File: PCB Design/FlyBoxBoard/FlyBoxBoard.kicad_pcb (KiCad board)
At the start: 2 copper layers, 40 parts, among them J1 5V in from buck converter, J10 R SCREW TERMINAL, J11 G SCREW TERMINAL, J12 W SCREW TERMINAL, J13 IR SCREW TERMINAL, J14 LCD Screen, J15 SD card reader, J16 Resistor, J17 Resistor, J18 ESP 32 Left Side extra pinouts, J19 ESP 32 Left Side extra pinouts, J2 12V in from buck converter, J20 Transistor, J21 Logic Level LV pinouts, J22 Potentiometer, J23 Logic Level Left Side LV, J24 ESP 32 Right Side extra pinou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, J25 ESP 32 Right Side extra pinou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, J26 BuckPuck IR, J27 Logic Level Right Side HV, J28 Logic Level HV pinouts, J29 Resistor, J3 ESP 32 Left Side, J30 Resistor, J31 Resistor, J32 Resistor, J33 Resistor, J34 Resistor, J35 Transistor, J36 Transistor, J37 Transistor, J38 BuckPuck White, J39 BuckPuck Green, J4 Real Time Controller, J40 BuckPuck Red, J5 ESP 32 Right Side, J6 Extra pinouts 5V, J7 Extra pinouts 12V, J8 Extra pinouts GND, J9 FAN SCREW TERMINAL

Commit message: PCB progress
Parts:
- J16, J17, J29, J30, J31, J32, J33, J34: footprint Connector_PinSocket_2.54mm:PinSocket_1x02_P2.54mm_Vertical -> Connector_PinSocket_2.54mm:PinSocket_1x05_P2.54mm_Vertical
- moved J10 322.2 mm to (67.3, 22.9)
- moved J11 322.2 mm to (61.0, 21.6)
- moved J12 322.2 mm to (74.9, 20.3)
- moved J13 236.1 mm to (168.9, -74.9)
- moved J9 141.0 mm to (24.1, 29.2), turned to 90 degrees
- moved J30 119.4 mm to (115.6, 37.4)
- moved J35 118.2 mm to (133.4, 39.9)
- moved J38 117.9 mm to (144.8, 36.1)
- moved J37 115.7 mm to (133.3, 83.1)
- moved J33 115.6 mm to (120.7, 80.5)
- moved J34 114.6 mm to (115.6, 80.5)
- moved J40 114.4 mm to (144.8, 79.5)
- moved J29 112.6 mm to (120.7, 37.4)
- moved J1 108.1 mm to (133.3, 17.8)
- moved J20 86.6 mm to (129.5, 105.9)
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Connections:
- J16 pad 2: Net-(J16-Pad2) -> unconnected-(J16-Pad2)
- J17 pad 2: /HV4 -> unconnected-(J17-Pad2)
- J20 pad 3: Net-(J16-Pad2) -> Net-(J20-Pad3)
- J22 pad 2: Net-(J16-Pad2) -> Net-(J20-Pad3)
- J22 pad 3: Net-(J16-Pad2) -> Net-(J20-Pad3)
- J26 pad 4: Net-(J16-Pad2) -> Net-(J20-Pad3)
- J27 pad 2: /LV1 -> /HV1
- J29 pad 2: Net-(J29-Pad2) -> unconnected-(J29-Pad2)
- J30 pad 2: /HV1 -> unconnected-(J30-Pad2)
- J31 pad 2: Net-(J31-Pad2) -> unconnected-(J31-Pad2)
- J32 pad 2: /HV2 -> unconnected-(J32-Pad2)
- J33 pad 2: Net-(J33-Pad2) -> unconnected-(J33-Pad2)
- J34 pad 2: /HV3 -> unconnected-(J34-Pad2)
- J35 pad 3: Net-(J29-Pad2) -> Net-(J35-Pad3)
- J36 pad 3: Net-(J31-Pad2) -> Net-(J36-Pad3)
- J37 pad 3: Net-(J33-Pad2) -> Net-(J37-Pad3)
- J38 pad 4: Net-(J29-Pad2) -> Net-(J35-Pad3)
- J39 pad 4: Net-(J31-Pad2) -> Net-(J36-Pad3)
- J40 pad 4: Net-(J33-Pad2) -> Net-(J37-Pad3)
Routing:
- net /GND: track 0.00 -> 48.0 mm
- net Net-(J16-Pad2): track 44.3 -> 0.00 mm
- net Net-(J20-Pad3): track 0.00 -> 28.7 mm
- net Net-(J37-Pad3): track 0.00 -> 26.1 mm
- net Net-(J36-Pad3): track 0.00 -> 25.7 mm
- net Net-(J35-Pad3): track 0.00 -> 25.7 mm
- net Net-(J20-Pad2): track 0.00 -> 19.9 mm
- net Net-(J36-Pad2): track 0.00 -> 19.9 mm
- net Net-(J35-Pad2): track 0.00 -> 19.9 mm
- net Net-(J34-Pad1): track 0.00 -> 19.9 mm
- net Net-(J37-Pad1): track 0.00 -> 13.1 mm
- net Net-(J35-Pad1): track 0.00 -> 12.0 mm
- net Net-(J36-Pad1): track 0.00 -> 12.0 mm
- net Net-(J20-Pad1): track 25.9 -> 15.8 mm
- net Net-(J24-Pad3): track 6.59 -> 10.4 mm
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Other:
- board outline added: 149.9 x 120.6 mm

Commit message: Main PCB complete
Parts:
- moved J13 157.3 mm to (45.7, 22.9), turned to -90 degrees
- moved J8 12.7 mm to (91.5, 44.5)
- moved J15 11.7 mm to (57.1, 129.5), turned to -90 degrees
- moved J7 11.4 mm to (63.5, 44.5)
- moved J6 11.4 mm to (78.8, 44.5)
- moved J10 10.2 mm to (57.1, 22.9), turned to -90 degrees
- moved J11 7.73 mm to (68.6, 22.9), turned to -90 degrees
- moved J4 7.41 mm to (31.8, 54.6)
- moved J9 6.48 mm to (22.9, 22.8)
- moved J12 5.68 mm to (80.0, 22.9), turned to -90 degrees
- moved J14 2.62 mm to (77.5, 129.5)
- moved J1 2.54 mm to (133.3, 20.3)
- moved J2 2.54 mm to (111.8, 20.3)
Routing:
- net /5V: track 0.00 -> 358.7 mm, vias 0 -> 2
- net /12V: track 0.00 -> 297.1 mm
- net /3V3: track 0.00 -> 175.1 mm
- net /IR LED-: track 0.00 -> 157.1 mm, vias 0 -> 2
- net /IR LED+: track 0.00 -> 153.5 mm, vias 0 -> 2
- net /HV5: track 0.00 -> 132.2 mm
- net /R LED-: track 0.00 -> 128.2 mm, vias 0 -> 2
- net /R LED+: track 0.00 -> 124.9 mm, vias 0 -> 2
- net /D22: track 0.00 -> 119.9 mm, vias 0 -> 4
- net /D21: track 0.00 -> 115.3 mm, vias 0 -> 4
- net /G LED-: track 0.00 -> 96.4 mm, vias 0 -> 2
- net /G LED+: track 0.00 -> 93.4 mm, vias 0 -> 2
- net /W LED-: track 0.00 -> 74.6 mm, vias 0 -> 2
- net /W LED+: track 0.00 -> 71.8 mm, vias 0 -> 2
- net /HV1: track 0.00 -> 57.1 mm, vias 0 -> 2
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- added copper zone on B.Cu, net /GND
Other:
- board size 149.9 x 120.6 mm -> 148.6 x 119.4 mm
- board text added: "ESP 32"

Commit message: Finished IR and RGW board
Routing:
- net /3V3: track 175.1 -> 173.0 mm
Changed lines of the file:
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@@
     (pts (xy 31.5268 81.5882) (xy 56.9268 81.5882))
     (height -5.08)
-    (gr_text "25.4000 mm" (at 44.2268 74.7082) (layer "F.Fab")
+    (gr_text "1000.0000 mils" (at 44.2268 74.7082) (layer "F.Fab")
       (effects (font (size 1.5 1.5) (thickness 0.3)))
     )
@@
     (pts (xy 86.36 91.44) (xy 99.06 91.44))
     (height -6.35)
-    (gr_text "12.7000 mm" (at 92.71 83.94) (layer "F.Fab")
+    (gr_text "500.0000 mils" (at 92.71 83.94) (layer "F.Fab")
       (effects (font (size 1 1) (thickness 0.15)))
     )
@@
   (segment (start 114.3 17.78) (end 147.32 17.78) (width 0.635) (layer "F.Cu") (net 3))
   (segment (start 109.22 17.78) (end 111.76 20.32) (width 0.635) (layer "F.Cu") (net 3))
-  (segment (start 91.44 91.44) (end 86.36 91.44) (width 0.635) (layer "F.Cu") (net 4))
   (segment (start 76.2 123.19) (end 85.09 123.19) (width 0.635) (layer "F.Cu") (net 4))
   (segment (start 86.36 118.11) (end 86.36 114.3) (width 0.635) (layer "F.Cu") (net 4))
   (segment (start 58.42 130.81) (end 58.42 132.08) (width 0.635) (layer "F.Cu") (net 4))
-  (segment (start 92.71 92.71) (end 91.44 91.44) (width 0.635) (layer "F.Cu") (net 4))
+  (segment (start 92.71 110.8964) (end 92.71 92.71) (width 0.635) (layer "F.Cu") (net 4))
   (segment (start 58.42 132.08) (end 71.12 132.08) (width 0.635) (layer "F.Cu") (net 4))
   (segment (start 71.12 132.08) (end 74.93 128.27) (width 0.635) (layer "F.Cu") (net 4))
+  (segment (start 91.44 91.44) (end 86.36 91.44) (width 0.635) (layer "F.Cu") (net 4))
   (segment (start 19.05 120.65) (end 19.05 83.82) (width 0.635) (layer "F.Cu") (net 4))
   (segment (start 85.09 123.19) (end 86.36 121.92) (width 0.635) (layer "F.Cu") (net 4))
-  (segment (start 92.71 111.76) (end 92.71 92.71) (width 0.635) (layer "F.Cu") (net 4))
   (segment (start 74.93 128.27) (end 74.93 124.46) (width 0.635) (layer "F.Cu") (net 4))
-  (segment (start 86.36 118.11) (end 92.71 111.76) (width 0.635) (layer "F.Cu") (net 4))
+  (segment (start 89.3064 114.3) (end 92.71 110.8964) (width 0.635) (layer "F.Cu") (net 4))
   (segment (start 19.05 83.82) (end 21.59 81.28) (width 0.635) (layer "F.Cu") (net 4))
   (segment (start 86.36 121.92) (end 86.36 118.11) (width 0.635) (layer "F.Cu") (net 4))
+  (segment (start 86.36 114.3) (end 89.3064 114.3) (width 0.635) (layer "F.Cu") (net 4))
   (segment (start 52.336961 132.7245) (end 31.1245 132.7245) (width 0.635) (layer "F.Cu") (net 4))
   (segment (start 31.2186 81.28) (end 31.5268 81.5882) (width 0.635) (layer "F.Cu") (net 4))
@@
   (segment (start 74.93 124.46) (end 76.2 123.19) (width 0.635) (layer "F.Cu") (net 4))
   (segment (start 52.981461 132.08) (end 52.336961 132.7245) (width 0.635) (layer "F.Cu") (net 4))
+  (segment (start 92.71 92.71) (end 91.44 91.44) (width 0.635) (layer "F.Cu") (net 4))
   (segment (start 58.42 132.08) (end 52.981461 132.08) (width 0.635) (layer "F.Cu") (net 4))
   (segment (start 57.15 129.54) (end 58.42 130.81) (width 0.635) (layer "F.Cu") (net 4))

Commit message: Ordering Fixes
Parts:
- moved J8 3.81 mm to (91.5, 48.3)
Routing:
- net /12V: track 297.1 -> 294.1 mm
- net /5V: track 358.7 -> 360.1 mm

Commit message: Update FlyBoxBoard.kicad_pcb
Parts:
- J1: value 5V in from buck converter -> 5V in
- J10: value R SCREW TERMINAL -> RED
- J11: value G SCREW TERMINAL -> GREEN
- J12: value W SCREW TERMINAL -> WHITE
- J13: value IR SCREW TERMINAL -> INFRARED
- J14: value LCD Screen -> LCD
- J18: value ESP 32 Left Side extra pinouts -> ESP 32 Left Side extra pins
- J2: value 12V in from buck converter -> 12V in
- J28: value Logic Level HV pinouts -> Logic Level HV pins
- J9: value FAN SCREW TERMINAL -> FAN
- moved GND 3.81 mm to (91.5, 44.5)
- renumbered J7 to 12V, J6 to 5V, J8 to GND
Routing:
- net /5V: track 360.1 -> 339.0 mm
- net /HV5: track 132.2 -> 127.1 mm
- net /HV4: track 29.0 -> 24.2 mm
- net Net-(J20-Pad2): track 19.9 -> 16.6 mm
- net /IR LED-: track 157.1 -> 158.9 mm
- net /IR LED+: track 153.5 -> 154.8 mm
- net /12V: track 294.1 -> 293.2 mm
- net /D23: track 31.2 -> 30.4 mm
- net /D22: track 119.9 -> 120.7 mm
- net /W LED+: track 71.8 -> 71.0 mm

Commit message: Gerber Files
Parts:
- J16, J17, J29, J30, J31, J32, J33, J34: value Resistor -> 5K Ohms
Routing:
- net (no net): track 0.00 -> 12.7 mm
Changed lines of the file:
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@@
       (disableapertmacros false)
       (usegerberextensions false)
-      (usegerberattributes true)
+      (usegerberattributes false)
       (usegerberadvancedattributes true)
       (creategerberjobfile true)
@@
       (outputformat 1)
       (mirror false)
-      (drillshape 1)
+      (drillshape 0)
       (scaleselection 1)
-      (outputdirectory "")
+      (outputdirectory "../FlyBoxBoardGerber/")
     )
   )
@@
       (effects (font (size 1 1) (thickness 0.15)))
     )
-    (fp_text value "Resistor" (at 0 12.93) (layer "F.SilkS")
+    (fp_text value "5K Ohms" (at 0 12.93) (layer "F.SilkS")
       (effects (font (size 1 1) (thickness 0.15)))
     )
@@
       (effects (font (size 1 1) (thickness 0.15)))
     )
-    (fp_text value "Resistor" (at 0 12.93) (layer "F.SilkS")
+    (fp_text value "5K Ohms" (at 0 12.93) (layer "F.SilkS")
       (effects (font (size 1 1) (thickness 0.15)))
     )
@@
       (effects (font (size 1 1) (thickness 0.15)))
     )
-    (fp_text value "Resistor" (at -3.835 4.5362 90) (layer "F.SilkS")
+    (fp_text value "5K Ohms" (at -3.835 4.5362 90) (layer "F.SilkS")
       (effects (font (size 1 1) (thickness 0.15)))
     )
@@
       (effects (font (size 1 1) (thickness 0.15)))
     )
-    (fp_text value "Resistor" (at 0 12.7) (layer "F.SilkS")
+    (fp_text value "5K Ohms" (at 0 12.7) (layer "F.SilkS")
       (effects (font (size 1 1) (thickness 0.15)))
     )
@@
       (effects (font (size 1 1) (thickness 0.15)))
     )
-    (fp_text value "ESP 32 Right Side extra pinouts" (at 3.785 7.3118 -90) (layer "F.SilkS")
+    (fp_text value "ESP 32 Right Side extra pinouts" (at 3.15 -7.2932 -90) (layer "F.SilkS")
       (effects (font (size 1 1) (thickness 0.15)))
     )
@@
     (property "Sheetname" "")
     (attr through_hole)
-    (fp_text reference "J4" (at 0 -2.77) (layer "F.SilkS")
-      (effects (font (size 1 1) (thickness 0.15)))
-    )
-    (fp_text value "Real Time Controller" (at 0 15.47) (layer "F.Fab")
+    (fp_text reference "J4" (at 0 -2.77) (layer "F.Fab")
+      (effects (font (size 1 1) (thickness 0.15)))
+    )
+    (fp_text value "Real Time Controller" (at 13.31 6.325) (layer "F.SilkS")
       (effects (font (size 1 1) (thickness 0.15)))
     )
@@
       (effects (font (size 1 1) (thickness 0.15)))
     )
-    (fp_text value "Extra pinouts GND" (at 0 12.93) (layer "F.Fab")
+    (fp_text value "Extra pinouts GND" (at 1.88 12.93) (layer "F.Fab")
       (effects (font (size 1 1) (thickness 0.15)))
     )
@@
       (effects (font (size 1 1) (thickness 0.15)))
     )
-    (fp_text value "Resistor" (at -3.835 5.05 90) (layer "F.SilkS")
+    (fp_text value "5K Ohms" (at -3.2 5.05 90) (layer "F.SilkS")
       (effects (font (size 1 1) (thickness 0.15)))
     )
@@
       (effects (font (size 1 1) (thickness 0.15)))
     )
-    (fp_text value "Resistor" (at 0 12.93) (layer "F.SilkS")
+    (fp_text value "5K Ohms" (at 0 12.93) (layer "F.SilkS")
       (effects (font (size 1 1) (thickness 0.15)))
     )
@@
       (effects (font (size 1 1) (thickness 0.15)))
     )
-    (fp_text value "Resistor" (at -2.565 3.81 90) (layer "F.SilkS")
+    (fp_text value "5K Ohms" (at -2.565 3.81 90) (layer "F.SilkS")
       (effects (font (size 1 1) (thickness 0.15)))
     )
@@
       (effects (font (size 1 1) (thickness 0.15)))
     )
-    (fp_text value "Resistor" (at -3.81 5.08 90) (layer "F.SilkS")
+    (fp_text value "5K Ohms" (at -3.81 5.08 90) (layer "F.SilkS")
       (effects (font (size 1 1) (thickness 0.15)))
     )
@@
     (pts (xy 31.5268 81.5882) (xy 56.9268 81.5882))
     (height -5.08)
-    (gr_text "1000.0000 mils" (at 44.2268 74.7082) (layer "F.Fab")
+    (gr_text "25.4000 mm" (at 44.2268 74.7082) (layer "F.Fab")
       (effects (font (size 1.5 1.5) (thickness 0.3)))
     )
@@
     (pts (xy 86.36 91.44) (xy 99.06 91.44))
     (height -6.35)
-    (gr_text "500.0000 mils" (at 92.71 83.94) (layer "F.Fab")
+    (gr_text "12.7000 mm" (at 92.71 83.94) (layer "F.Fab")
       (effects (font (size 1 1) (thickness 0.15)))
     )
@@
     (style (thickness 0.1) (arrow_length 1.27) (text_position_mode 0) (extension_height 0.58642) (extension_offset 0.5) keep_text_aligned)
   )
+  (segment (start 113.665 130.175) (end 114.3 129.54) (width 0.25) (layer "F.Cu") (net 0))
+  (segment (start 115.57 129.54) (end 116.205 129.54) (width 0.25) (layer "F.Cu") (net 0))
+  (segment (start 116.205 129.54) (end 116.205 130.81) (width 0.25) (layer "F.Cu") (net 0))
+  (segment (start 116.205 129.54) (end 116.84 129.54) (width 0.25) (layer "F.Cu") (net 0))
+  (segment (start 114.935 130.175) (end 114.3 130.81) (width 0.25) (layer "F.Cu") (net 0))
+  (segment (start 117.475 130.81) (end 118.11 130.81) (width 0.25) (layer "F.Cu") (net 0))
+  (segment (start 117.475 129.54) (end 118.11 129.54) (width 0.25) (layer "F.Cu") (net 0))
+  (segment (start 118.11 130.81) (end 118.745 130.175) (width 0.25) (layer "F.Cu") (net 0))
+  (segment (start 114.3 130.81) (end 113.665 130.175) (width 0.25) (layer "F.Cu") (net 0))
+  (segment (start 118.11 129.54) (end 118.11 130.175) (width 0.25) (layer "F.Cu") (net 0))
+  (segment (start 118.745 130.175) (end 117.475 130.175) (width 0.25) (layer "F.Cu") (net 0))
+  (segment (start 117.475 129.54) (end 117.475 130.81) (width 0.25) (layer "F.Cu") (net 0))
+  (segment (start 115.57 130.81) (end 115.57 130.175) (width 0.25) (layer "F.Cu") (net 0))
+  (segment (start 114.3 129.54) (end 114.935 130.175) (width 0.25) (layer "F.Cu") (net 0))
+  (segment (start 116.205 130.81) (end 115.57 130.81) (width 0.25) (layer "F.Cu") (net 0))
   (segment (start 80.01 129.54) (end 80.01 130.81) (width 0.635) (layer "F.Cu") (net 2))
   (segment (start 18.034 124.714) (end 18.034 81.026) (width 0.635) (layer "F.Cu") (net 2))
@@
   (segment (start 71.12 62.23) (end 74.93 62.23) (width 0.635) (layer "F.Cu") (net 2))
   (segment (start 128.6 27.55) (end 133.29 22.86) (width 0.635) (layer "F.Cu") (net 2))
+  (segment (start 76.213417 60.946583) (end 76.213417 57.164083) (width 0.635) (layer "F.Cu") (net 2))
+  (segment (start 78.7375 54.64) (end 78.765 54.64) (width 0.635) (layer "F.Cu") (net 2))
   (segment (start 56.9268 76.2308) (end 56.9268 76.4232) (width 0.635) (layer "F.Cu") (net 2))
   (segment (start 80.01 130.81) (end 76.454 134.366) (width 0.635) (layer "F.Cu") (net 2))
-  (segment (start 78.765 54.64) (end 78.7375 54.64) (width 0.635) (layer "F.Cu") (net 2))
-  (segment (start 76.226834 60.96) (end 76.213417 60.946583) (width 0.635) (layer "F.Cu") (net 2))
   (segment (start 56.9268 76.4232) (end 56.9268 81.5882) (width 0.635) (layer "F.Cu") (net 2))
   (segment (start 103.170868 27.55) (end 128.6 27.55) (width 0.635) (layer "F.Cu") (net 2))
@@
   (segment (start 98.970868 31.75) (end 103.170868 27.55) (width 0.635) (layer "F.Cu") (net 2))
   (segment (start 133.29 22.86) (end 133.35 22.86) (width 0.635) (layer "F.Cu") (net 2))
-  (segment (start 76.213417 57.164083) (end 76.213417 60.946583) (width 0.635) (layer "F.Cu") (net 2))
+  (segment (start 76.213417 57.164083) (end 78.7375 54.64) (width 0.635) (layer "F.Cu") (net 2))
   (segment (start 18.034 81.026) (end 22.86 76.2) (width 0.635) (layer "F.Cu") (net 2))
   (segment (start 87.540868 31.75) (end 98.970868 31.75) (width 0.635) (layer "F.Cu") (net 2))
-  (segment (start 78.7375 54.64) (end 76.213417 57.164083) (width 0.635) (layer "F.Cu") (net 2))
   (segment (start 81.026 63.246) (end 81.026 56.901) (width 0.635) (layer "F.Cu") (net 2))
   (segment (start 99.06 91.44) (end 99.06 81.28) (width 0.635) (layer "F.Cu") (net 2))
@@
   (segment (start 106.6142 106.74) (end 106.68 106.8058) (width 0.254) (layer "F.Cu") (net 51))
   (segment (start 99.06 106.68) (end 99.12 106.74) (width 0.254) (layer "F.Cu") (net 51))
-  (segment (start 99.12 106.74) (end 106.6142 106.74) (width 0.254) (layer "F.Cu") (net 51))
-  (segment (start 99.12 109.28) (end 106.6142 109.28) (width 0.254) (layer "F.Cu") (net 52))
+  (segment (start 99.12 106.74) (end 106.6142 106.74) (width 0.635) (layer "F.Cu") (net 51))
+  (segment (start 99.12 109.28) (end 106.6142 109.28) (width 0.635) (layer "F.Cu") (net 52))
   (segment (start 106.6142 109.28) (end 106.68 109.3458) (width 0.254) (layer "F.Cu") (net 52))
   (segment (start 99.06 109.22) (end 99.12 109.28) (width 0.254) (layer "F.Cu") (net 52))
-  (segment (start 99.12 111.82) (end 106.6142 111.82) (width 0.254) (layer "F.Cu") (net 53))
+  (segment (start 99.12 111.82) (end 106.6142 111.82) (width 0.635) (layer "F.Cu") (net 53))
   (segment (start 106.6142 111.82) (end 106.68 111.8858) (width 0.254) (layer "F.Cu") (net 53))
   (segment (start 99.06 111.76) (end 99.12 111.82) (width 0.254) (layer "F.Cu") (net 53))

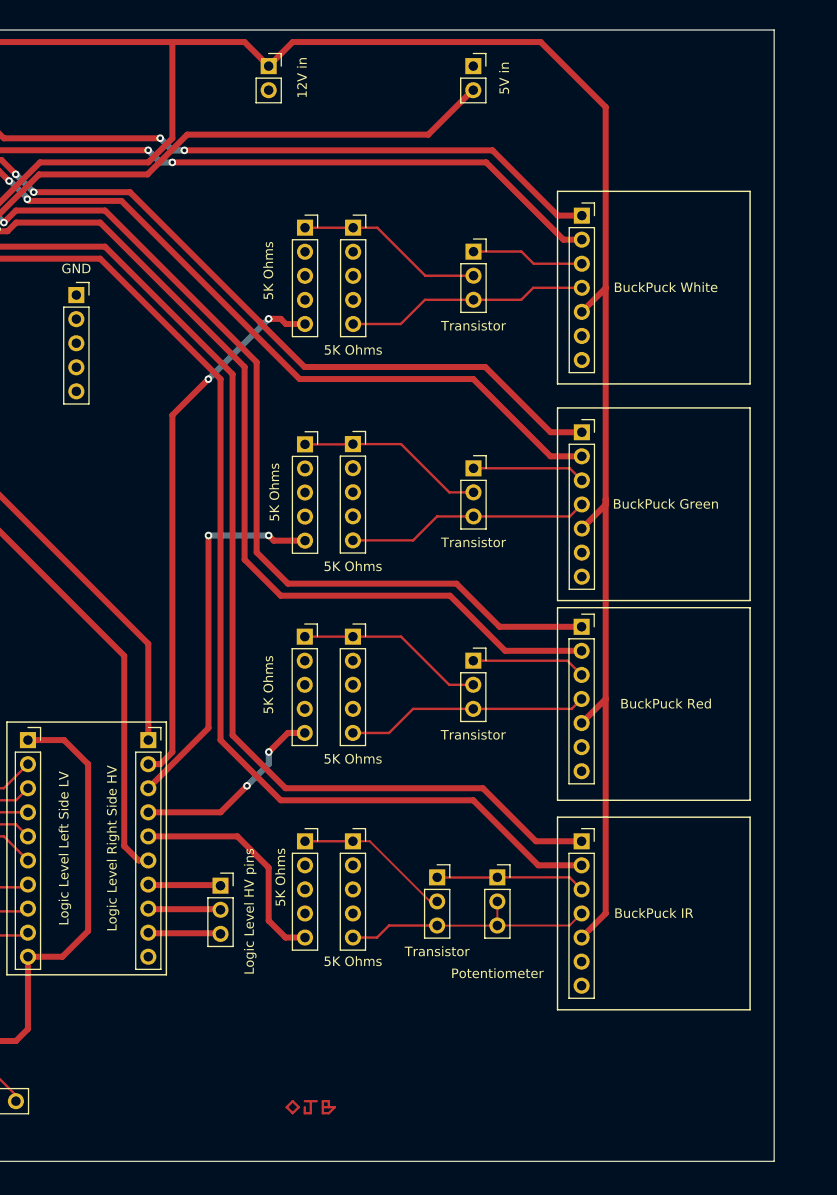
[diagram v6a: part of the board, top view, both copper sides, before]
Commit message: Logos and labels
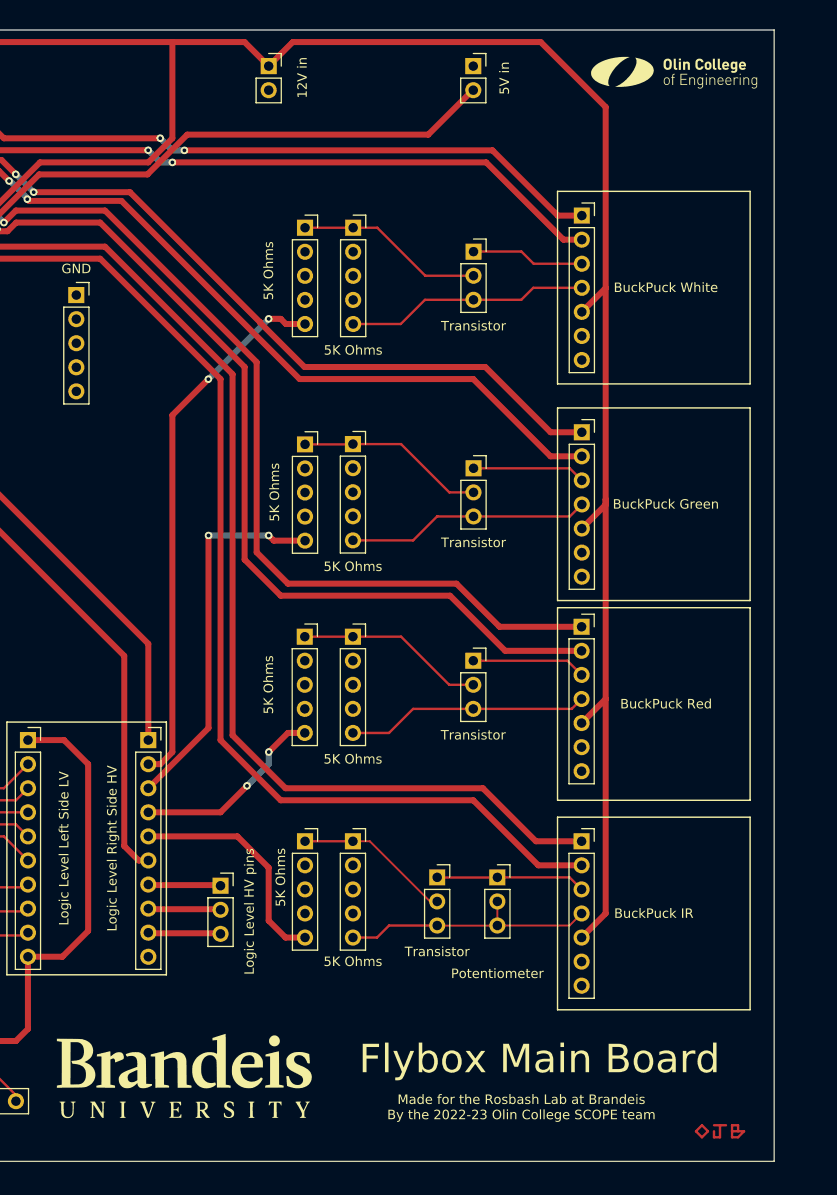
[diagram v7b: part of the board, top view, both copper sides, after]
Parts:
- added G***: LOGO, LOGO, F.Cu at (102.9, 127.0)
- added G***: LOGO, LOGO, F.Cu at (154.3, 21.0)
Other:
- board text added: "Flybox Main Board"
- board text added: "Made for the Rosbash Lab at Brandeis By the 2022-23 Olin College SCOPE team"
